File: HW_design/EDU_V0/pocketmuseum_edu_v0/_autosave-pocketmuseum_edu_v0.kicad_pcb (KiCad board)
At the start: 4 copper layers, 96.8 x 51 mm, 114 parts, among them J101 USB_C_Receptacle_USB2.0_16P, J102 JST PH S2B, J201 TF-015, J205 SM04B-SRSS-TB, J206 SM04B-SRSS-TB, Q301 BSS138, Q302 BSS138, Q303 BSS138, SW101 PTS810SJG250, SW201 PTS810SJG250, U101 BQ24040, U102 APX803-29SAG, U103 AP2112K-3.3, U104 AP2112K-1.8, U201 ESP32-C6-MINI-1/U, U301 ICM-20948, U302 ICP20100, U303 BH1750FVI, U304 T3902

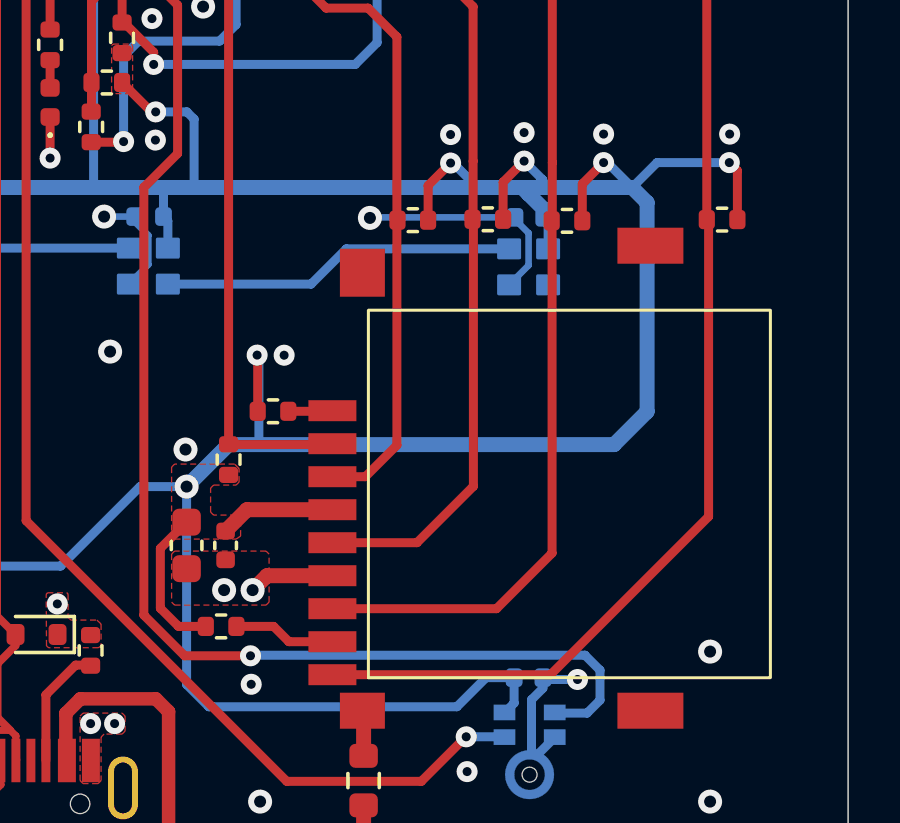
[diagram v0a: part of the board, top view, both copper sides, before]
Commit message: Fixed EDUV0 Missing Mask
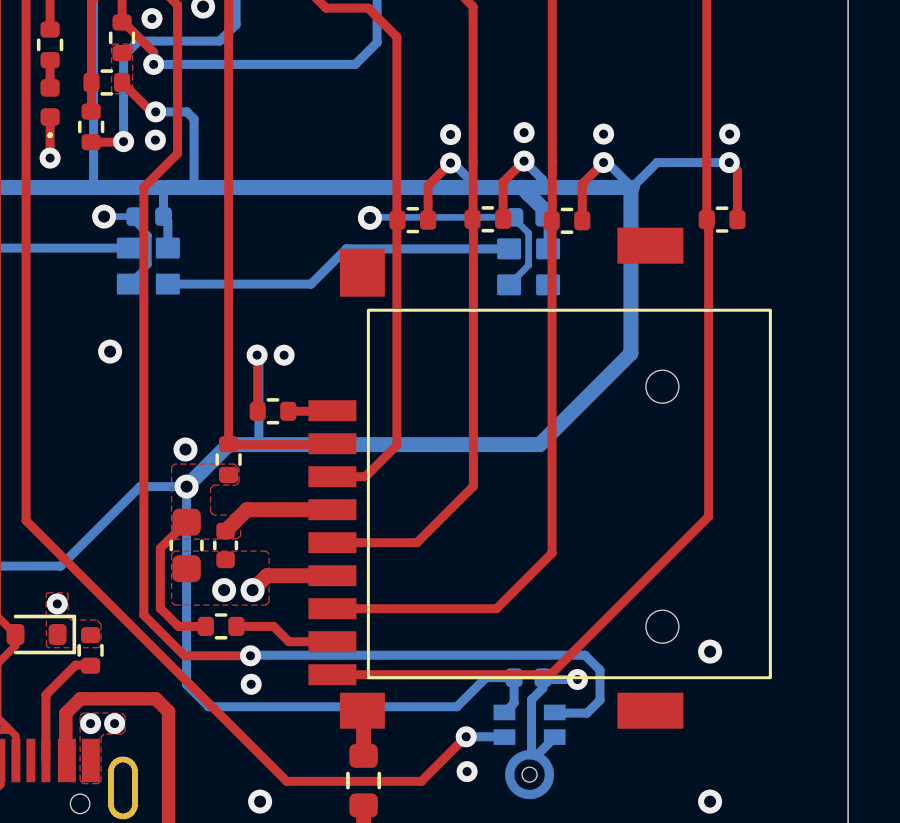
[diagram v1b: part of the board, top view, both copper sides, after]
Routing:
- net +3V3: track 337.6 -> 335.7 mm
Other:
- board text added: "LAB"
- board text removed: "MUSEUM"
